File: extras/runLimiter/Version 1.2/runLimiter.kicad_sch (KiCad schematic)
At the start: 9 parts, among them J1 5-20 Volts, J2 Vout, Q1 2N3904, Q1(alt)1 2SC1945, U1 78L03, U2 ESP8266-01s

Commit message: Modified directory structure
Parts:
- added J3: Dry Contacts, Connector_PinHeader_2.54mm:PinHeader_1x02_P2.54mm_Vertical, symbol Connector_TH_Headers:Conn_01x02
- added K1: Relay, Relay_THT:Relay_SPST_SANYOU_SRD_Series_Form_A, symbol Relay:SANYOU_SRD_Form_A
- Q2: renamed from Q1(alt)1; value 2SC1945 -> 2SD2023
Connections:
- net Control Ground: now also Q2.2 (C), K1.2; no longer Q2.3 (C)
- net Control Power: now also K1.5
- net GNDREF: now also Q2.3 (E); no longer Q2.2 (E)
- new net: J3.2 (Pin_2), K1.1
- new net: J3.1 (Pin_1), K1.3
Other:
- company: (none) -> OmniTronics
- title: (none) -> Run Time Limiter
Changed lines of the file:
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@@
 (kicad_sch (version 20211123) (generator eeschema)
   (paper "A4")
+  (title_block
+    (title "Run Time Limiter")
+    (date "2023-08-08")
+    (rev "1.2")
+    (company "OmniTronics")
+  )
+  (junction (at 189.23 57.15) (diameter 0) (color 0 0 0 0)
+  )
   (junction (at 175.895 109.22) (diameter 0) (color 0 0 0 0)
   )
@@
   )
   (junction (at 185.42 103.505) (diameter 0) (color 0 0 0 0)
+  )
+  (junction (at 202.565 103.505) (diameter 0) (color 0 0 0 0)
   )
   (no_connect (at 173.355 81.28))
@@
   (no_connect (at 125.095 86.36))
   (no_connect (at 173.355 83.82))
+  (wire (pts (xy 210.82 103.505) (xy 202.565 103.505))
+    (stroke (width 0) (type default) (color 0 0 0 0))
+  )
+  (wire (pts (xy 210.82 97.155) (xy 210.82 103.505))
+    (stroke (width 0) (type default) (color 0 0 0 0))
+  )
   (wire (pts (xy 94.615 76.2) (xy 98.425 76.2))
     (stroke (width 0) (type default) (color 0 0 0 0))
@@
     (stroke (width 0) (type default) (color 0 0 0 0))
   )
+  (wire (pts (xy 220.98 97.155) (xy 220.98 99.695))
+    (stroke (width 0) (type default) (color 0 0 0 0))
+  )
   (wire (pts (xy 189.23 78.105) (xy 185.42 78.105))
     (stroke (width 0) (type default) (color 0 0 0 0))
@@
     (stroke (width 0) (type default) (color 0 0 0 0))
   )
+  (wire (pts (xy 210.82 57.15) (xy 189.23 57.15))
+    (stroke (width 0) (type default) (color 0 0 0 0))
+  )
   (wire (pts (xy 120.65 83.82) (xy 125.095 83.82))
     (stroke (width 0) (type default) (color 0 0 0 0))
@@
     (stroke (width 0) (type default) (color 0 0 0 0))
   )
+  (wire (pts (xy 210.82 81.915) (xy 210.82 57.15))
+    (stroke (width 0) (type default) (color 0 0 0 0))
+  )
+  (wire (pts (xy 220.98 76.2) (xy 220.98 81.915))
+    (stroke (width 0) (type default) (color 0 0 0 0))
+  )
   (wire (pts (xy 202.565 120.015) (xy 202.565 103.505))
     (stroke (width 0) (type default) (color 0 0 0 0))
@@
     (stroke (width 0) (type default) (color 0 0 0 0))
   )
+  (wire (pts (xy 234.95 99.695) (xy 234.95 90.17))
+    (stroke (width 0) (type default) (color 0 0 0 0))
+  )
   (wire (pts (xy 167.64 109.22) (xy 116.84 109.22))
     (stroke (width 0) (type default) (color 0 0 0 0))
@@
     (stroke (width 0) (type default) (color 0 0 0 0))
   )
+  (wire (pts (xy 234.95 87.63) (xy 234.95 76.2))
+    (stroke (width 0) (type default) (color 0 0 0 0))
+  )
   (wire (pts (xy 98.425 57.15) (xy 98.425 64.77))
     (stroke (width 0) (type default) (color 0 0 0 0))
@@
     (stroke (width 0) (type default) (color 0 0 0 0))
   )
+  (wire (pts (xy 220.98 99.695) (xy 234.95 99.695))
+    (stroke (width 0) (type default) (color 0 0 0 0))
+  )
   (wire (pts (xy 172.72 109.22) (xy 175.895 109.22))
     (stroke (width 0) (type default) (color 0 0 0 0))
   )
   (wire (pts (xy 179.07 99.695) (xy 179.07 86.36))
+    (stroke (width 0) (type default) (color 0 0 0 0))
+  )
+  (wire (pts (xy 234.95 76.2) (xy 220.98 76.2))
     (stroke (width 0) (type default) (color 0 0 0 0))
   )
@@
     (pin "1")
   )
+  (symbol (lib_id "Relay:SANYOU_SRD_Form_A") (at 215.9 89.535 0) (unit 1)
+    (in_bom yes) (on_board yes) (fields_autoplaced)
+    (property "Reference" "K1" (id 0) (at 224.282 88.7003 0)
+      (effects (font (size 1.27 1.27)) (justify left))
+    )
+    (property "Value" "Relay" (id 1) (at 224.282 91.2372 0)
+      (effects (font (size 1.27 1.27)) (justify left) hide)
+    )
+    (property "Footprint" "Relay_THT:Relay_SPST_SANYOU_SRD_Series_Form_A" (id 2) (at 224.79 90.805 0)
+      (effects (font (size 1.27 1.27)) (justify left) hide)
+    )
+    (property "Datasheet" "http://www.sanyourelay.ca/public/products/pdf/SRD.pdf" (id 3) (at 215.9 89.535 0)
+      (effects (font (size 1.27 1.27)) hide)
+    )
+    (pin "1")
+    (pin "2")
+    (pin "3")
+    (pin "5")
+  )
   (symbol (lib_id "Device:LED") (at 156.21 99.695 0) (mirror x) (unit 1)
     (in_bom yes) (on_board yes) (fields_autoplaced)
@@
     (pin "2")
   )
+  (symbol (lib_id "Connector_TH_Headers:Conn_01x02") (at 240.03 87.63 0) (unit 1)
+    (in_bom yes) (on_board yes) (fields_autoplaced)
+    (property "Reference" "J3" (id 0) (at 242.062 88.0653 0)
+      (effects (font (size 1.27 1.27)) (justify left))
+    )
+    (property "Value" "Dry Contacts" (id 1) (at 242.062 90.6022 0)
+      (effects (font (size 1.27 1.27)) (justify left))
+    )
+    (property "Footprint" "Connector_PinHeader_2.54mm:PinHeader_1x02_P2.54mm_Vertical" (id 2) (at 240.03 87.63 0)
+      (effects (font (size 1.27 1.27)) hide)
+    )
+    (property "Datasheet" "~" (id 3) (at 240.03 87.63 0)
+      (effects (font (size 1.27 1.27)) hide)
+    )
+    (pin "1")
+    (pin "2")
+  )
   (symbol (lib_id "Transistor_BJT:2SC1945") (at 200.025 125.095 0) (unit 1)
-    (in_bom yes) (on_board yes) (fields_autoplaced)
-    (property "Reference" "Q1(alt)1" (id 0) (at 204.9018 124.2603 0)
-      (effects (font (size 1.27 1.27)) (justify left))
-    )
-    (property "Value" "2SC1945" (id 1) (at 204.9018 126.7972 0)
-      (effects (font (size 1.27 1.27)) (justify left))
-    )
-    (property "Footprint" "Package_TO_SOT_THT:TO-220-3_Vertical" (id 2) (at 205.105 127 0)
+    (in_bom yes) (on_board yes)
+    (property "Reference" "Q2" (id 0) (at 205.105 123.825 0)
+      (effects (font (size 1.27 1.27)) (justify left))
+    )
+    (property "Value" "2SD2023" (id 1) (at 205.105 126.365 0)
+      (effects (font (size 1.27 1.27)) (justify left))
+    )
+    (property "Footprint" "Package_TO_SOT_THT:TO-220-3_Vertical" (id 2) (at 203.2 130.81 0)
       (effects (font (size 1.27 1.27) italic) (justify left) hide)
     )
-    (property "Datasheet" "http://rtellason.com/transdata/2sc1945.pdf" (id 3) (at 200.025 125.095 0)
+    (property "Datasheet" "https://pdf1.alldatasheet.com/datasheet-pdf/view/271672/SAVANTIC/2SD2023.html" (id 3) (at 187.96 120.015 0)
       (effects (font (size 1.27 1.27)) (justify left) hide)
     )
@@
       (reference "J2") (unit 1) (value "Vout") (footprint "Connector_PinHeader_2.54mm:PinHeader_1x02_P2.54mm_Vertical")
     )
+    (path "/5eb2672e-47f8-4d76-910a-2089fe95bb23"
+      (reference "J3") (unit 1) (value "Dry Contacts") (footprint "Connector_PinHeader_2.54mm:PinHeader_1x02_P2.54mm_Vertical")
+    )
+    (path "/53dd8491-cda7-4e9d-b048-ada4398b4844"
+      (reference "K1") (unit 1) (value "Relay") (footprint "Relay_THT:Relay_SPST_SANYOU_SRD_Series_Form_A")
+    )
     (path "/1415e638-ddaf-427e-a966-dcc08fade057"
       (reference "Q1") (unit 1) (value "2N3904") (footprint "Package_TO_SOT_THT:TO-92_Inline")
     )
     (path "/7ee5bc87-a8f8-436d-b25b-b1224d905910"
-      (reference "Q1(alt)1") (unit 1) (value "2SC1945") (footprint "Package_TO_SOT_THT:TO-220-3_Vertical")
+      (reference "Q2") (unit 1) (value "2SD2023") (footprint "Package_TO_SOT_THT:TO-220-3_Vertical")
     )
     (path "/21bf4f50-a8d9-417b-ac0c-847097873399"

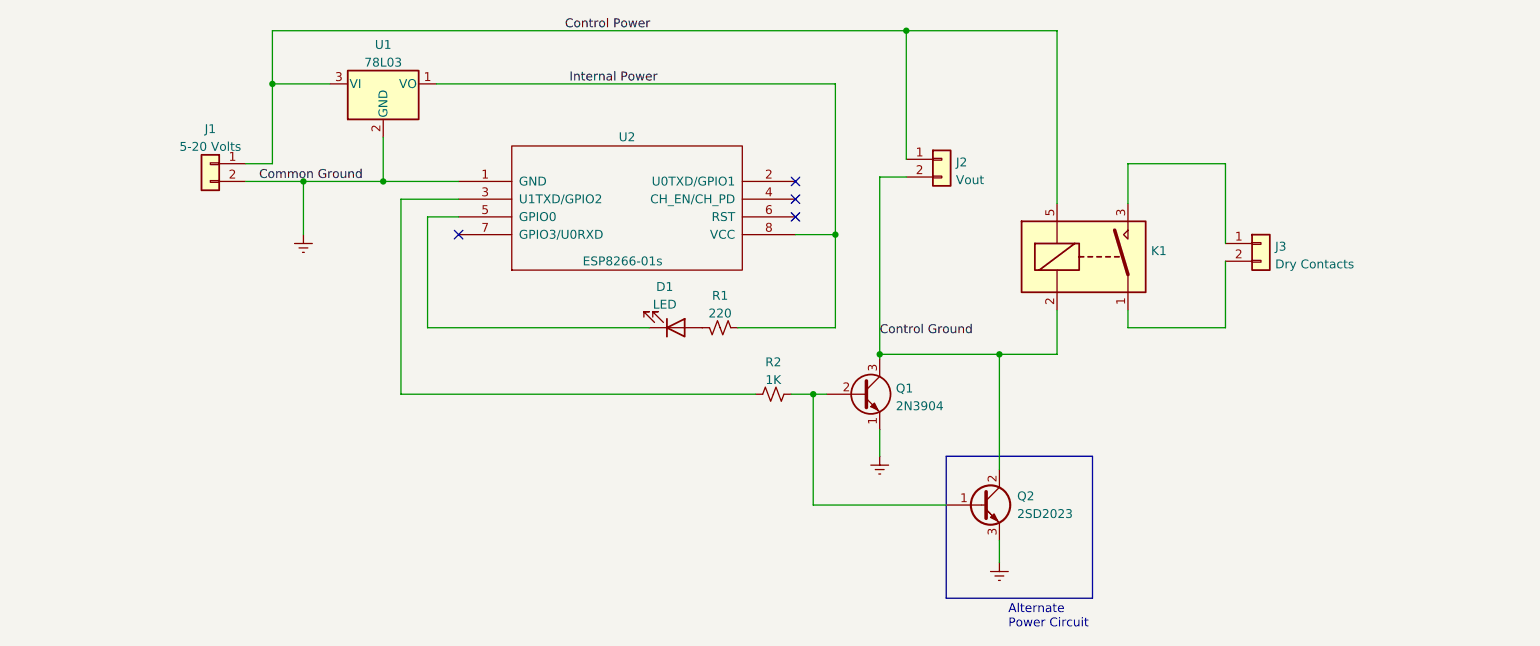
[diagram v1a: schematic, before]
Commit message: Moved power control from GPIO2 to GPIO3
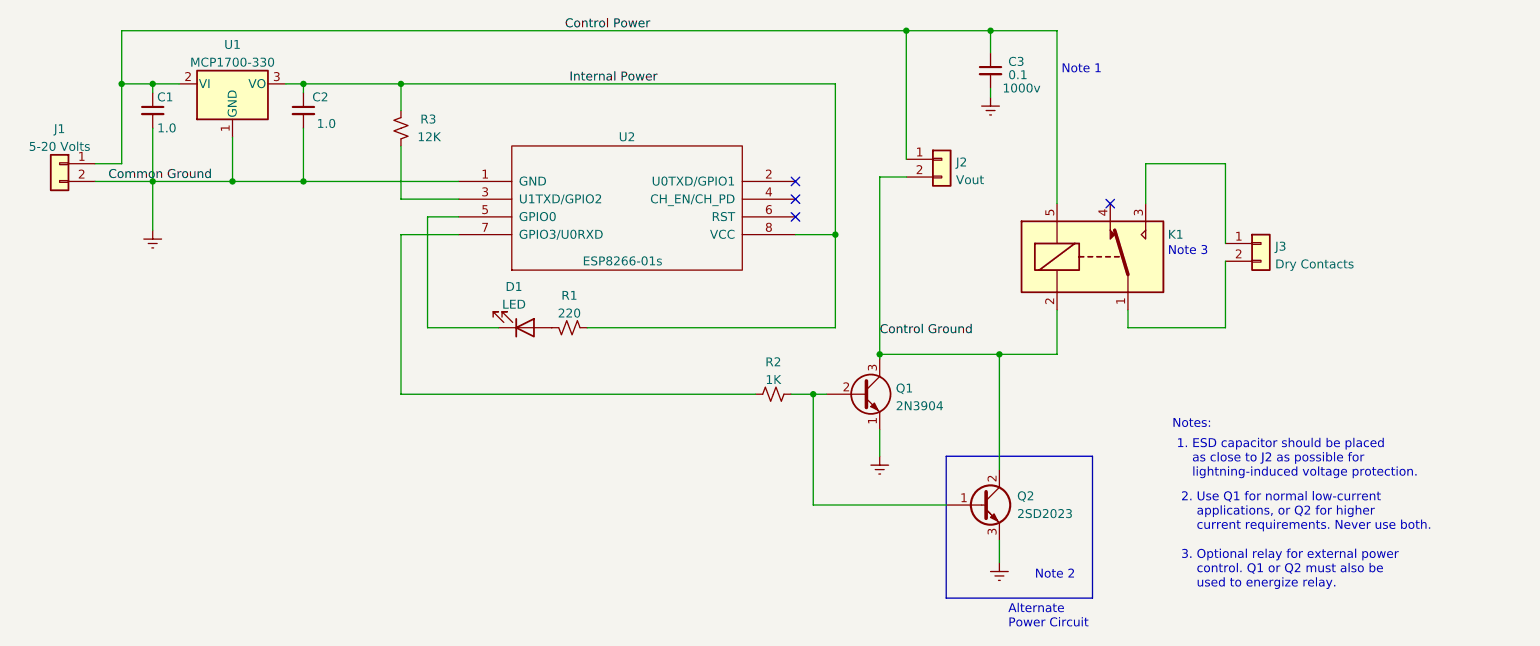
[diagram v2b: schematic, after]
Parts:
- removed U1: 78L03, Package_TO_SOT_THT:TO-92_Inline, symbol Regulator_Linear:L78L05_TO92
- added C1, C2: 1.0, Ferrite_THT:LairdTech_28C0236-0JW-10, symbol Device:C_Small
- added C3: 0.1, Capacitor_THT:C_Disc_D10.5mm_W5.0mm_P10.00mm, symbol Device:C_Small
- added R3: 12K, Resistor_THT:R_Axial_DIN0207_L6.3mm_D2.5mm_P10.16mm_Horizontal, symbol Device:R_Small_US
- added U1: MCP1700-330, Package_TO_SOT_THT:TO-92_Inline, symbol Regulator_Linear:MCP1700x-330xxTO
- K1: footprint Relay_THT:Relay_SPST_SANYOU_SRD_Series_Form_A -> Relay_THT:Relay_SPDT_SANYOU_SRD_Series_Form_C; symbol Relay:SANYOU_SRD_Form_A -> Relay:SANYOU_SRD_Form_C
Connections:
- net Control Power: now also C1.1, C3.1, U1.2 (VI)
- net GNDREF: now also C1.2, C2.2, C3.2, U1.1 (GND)
- net Internal Power: now also C2.1, R3.2, U1.3 (VO)
- net at R2.2: now also U2.7 (GPIO3/U0RXD); no longer U2.3 (U1TXD/GPIO2)
- new net: R3.1, U2.3 (U1TXD/GPIO2)
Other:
- note added: "1. ESD capacitor should be placed as close to J2 as possible for lightning-induced voltage protection."
- note added: "2. Use Q1 for normal low-current applications, or Q2 for higher current requirements. Never use both."
- note added: "3. Optional relay for external power control. Q1 or Q2 must also be used to energize relay."
- note added: "Note 1"
- note added: "Note 2"
- note added: "Note 3"
- note added: "Notes:"
- moved on the sheet: D1, J1, R1
